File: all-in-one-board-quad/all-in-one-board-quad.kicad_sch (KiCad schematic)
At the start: 33 parts, among them J1 Conn_01x06_Pin, J2 Conn_01x03_Pin, J3 Conn_01x06_Pin, J4 Conn_01x06_Pin, M1 VQ4TL2BQ380001, M2 VQ4TL2BQ380001, M3 VQ4TL2BQ380001, M4 VQ4TL2BQ380001, U1 Pico, U3 TB6612FNG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

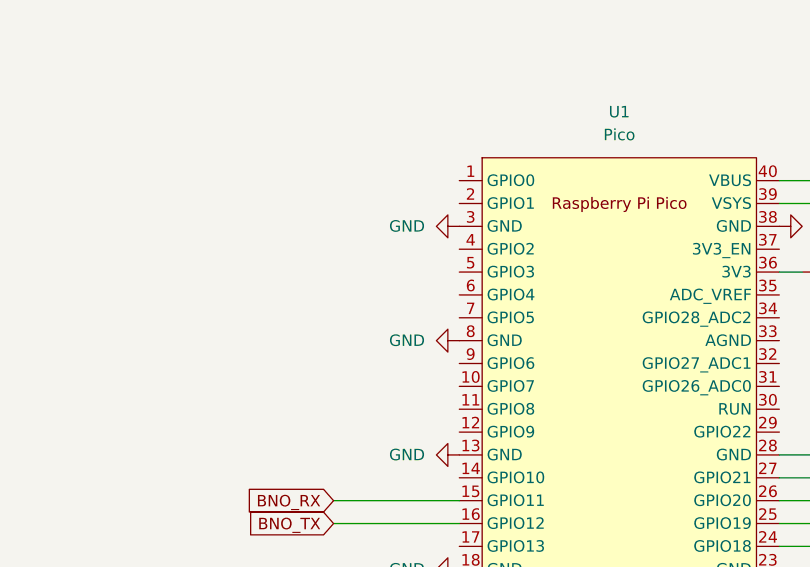
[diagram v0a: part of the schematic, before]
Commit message: update MCU to have pins for PWM to motors
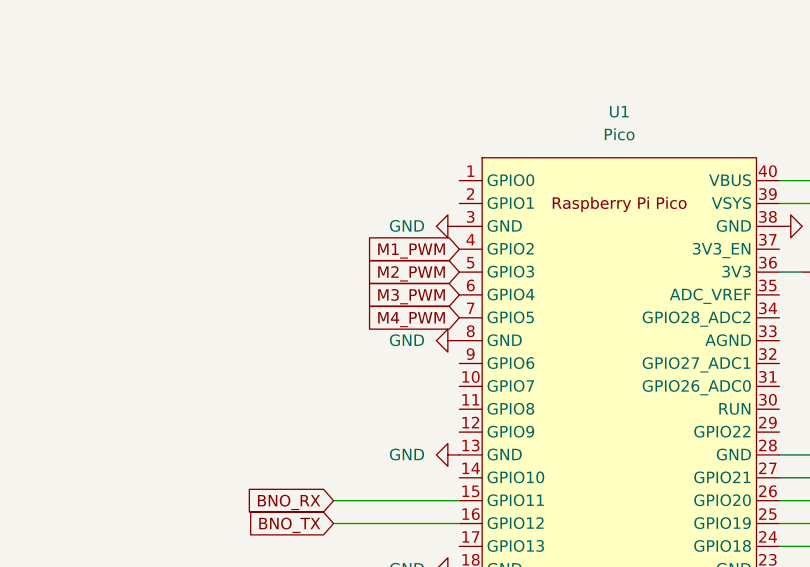
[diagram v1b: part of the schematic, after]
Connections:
- net M1_PWM: now also U1.4 (GPIO2)
- net M2_PWM: now also U1.5 (GPIO3)
- net M3_PWM: now also U1.6 (GPIO4)
- net M4_PWM: now also U1.7 (GPIO5)

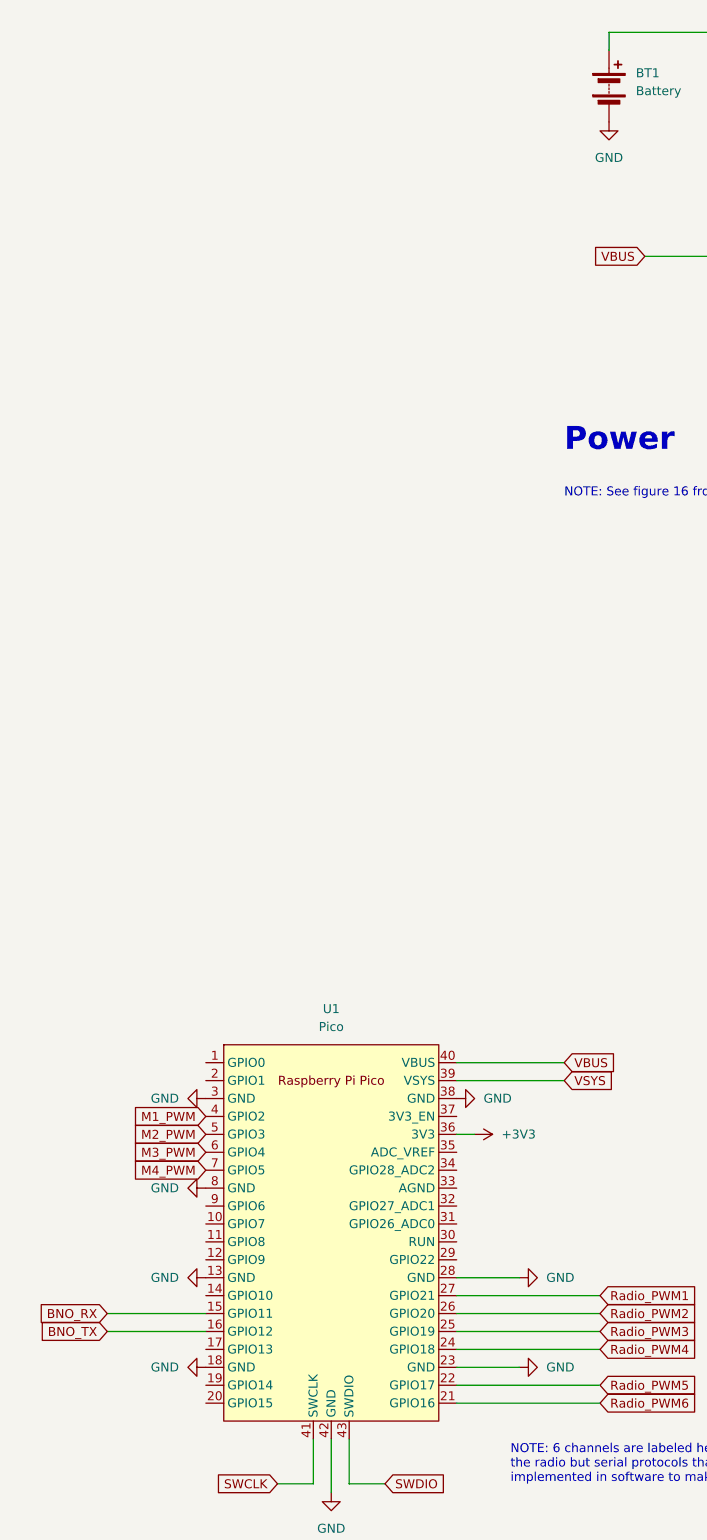
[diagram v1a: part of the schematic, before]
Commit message: add motor direction control to board
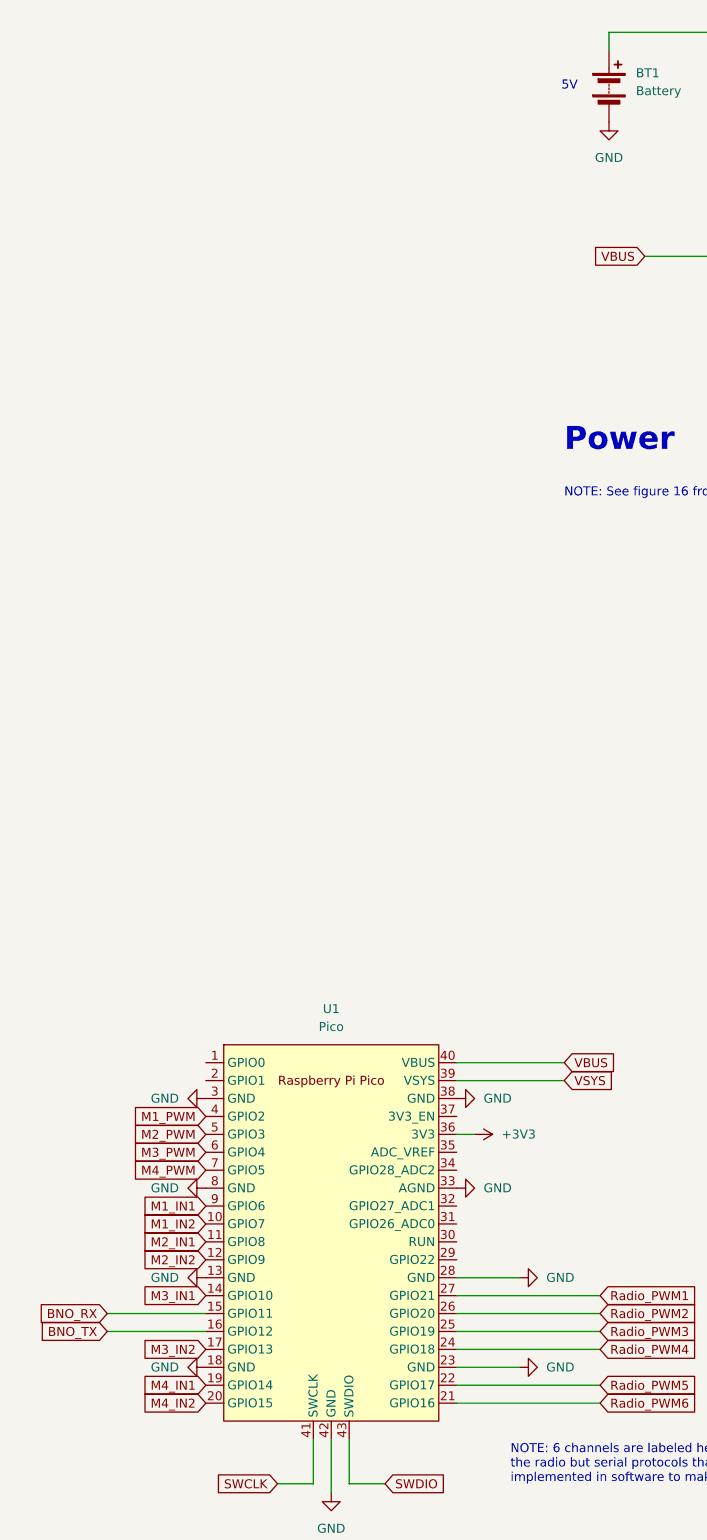
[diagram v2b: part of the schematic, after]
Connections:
- net GND: now also U1.33 (AGND)
- net M1_IN1: now also U1.9 (GPIO6)
- net M1_IN2: now also U1.10 (GPIO7)
- net M2_IN1: now also U1.11 (GPIO8)
- net M2_IN2: now also U1.12 (GPIO9)
- net M3_IN1: now also U1.14 (GPIO10)
- net M3_IN2: now also U1.17 (GPIO13)
- net M4_IN1: now also U1.19 (GPIO14)
- net M4_IN2: now also U1.20 (GPIO15)
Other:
- note added: "5V"
